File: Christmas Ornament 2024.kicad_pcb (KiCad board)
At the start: 2 copper layers, 76.2 x 76.2 mm, 80 parts, among them J1 USB_B_Micro, J2 Conn_01x03, J3 Conn_01x03, J4 Conn_01x03, J5 Conn_01x03, SW1 PTS815, SW2 PTS815, SW3 PTS815, SW4 PTS815, U1 RP2040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

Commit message: Layout in progress...
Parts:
- J2: footprint Connector_PinHeader_2.54mm:PinHeader_1x03_P2.54mm_Vertical -> Connector_JST:JST_SH_BM03B-SRSS-TB_1x03-1MP_P1.00mm_Vertical
- J3: footprint Connector_PinHeader_2.54mm:PinHeader_1x03_P2.54mm_Vertical -> Connector_PinHeader_1.27mm:PinHeader_1x03_P1.27mm_Vertical
- moved D7 113.1 mm to (93.0, 115.6)
- moved D8 106.8 mm to (113.5, 136.7)
- moved D5 101.2 mm to (90.2, 101.6)
- moved D6 100.1 mm to (101.1, 127.3)
- moved U3 96.4 mm to (115.3, 115.3), turned to 90 degrees
- moved D9 96.4 mm to (126.7, 138.2)
- moved D4 95.5 mm to (93.5, 87.9)
- moved D13 93.2 mm to (140.7, 135.6)
- moved U2 92.9 mm to (127.0, 101.6)
- moved R12 92.7 mm to (104.4, 123.7), turned to 135 degrees
- moved R13 91.3 mm to (97.5, 113.5), turned to 112.5 degrees
- moved R11 90.5 mm to (95.2, 101.3), turned to 90 degrees
- moved D3 86.3 mm to (101.6, 76.5)
- moved R14 85.5 mm to (114.8, 130.8), turned to 157.5 degrees
- moved R10 84.8 mm to (97.8, 89.4), turned to 67.5 degrees
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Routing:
- net GND: track 4.11 -> 42.4 mm
- net QSPI SS: track 0.00 -> 25.0 mm
- net QSPI SD1: track 0.00 -> 20.4 mm
- net QSPI SD2: track 0.00 -> 17.7 mm
- net SWD: track 0.00 -> 15.0 mm
- net SWCLK: track 0.00 -> 14.3 mm
- net QSPI SD3: track 0.00 -> 13.1 mm
- net QSPI SCLK: track 0.00 -> 11.5 mm
- net QSPI SD0: track 0.00 -> 10.5 mm
- net +BATT: track 3.41 -> 12.4 mm
- net TMP235 Out: track 0.00 -> 4.49 mm
- net +3V3: track 39.4 -> 42.6 mm
- net Net-(U5-V_{FB}): track 3.24 -> 4.95 mm
- net Net-(U1-USB_DP): track 4.46 -> 3.84 mm
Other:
- copper layers 2 -> 4

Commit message: PCB Layout and Routing complete
DRC
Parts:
- removed J3: Conn_01x03, Connector_PinHeader_1.27mm:PinHeader_1x03_P1.27mm_Vertical
- added D18: Green LED, LED_SMD:LED_0805_2012Metric_Pad1.15x1.40mm_HandSolder, F.Cu at (124.8, 91.7)
- added R24: 100, Resistor_SMD:R_0805_2012Metric_Pad1.20x1.40mm_HandSolder, F.Cu at (128.9, 91.7)
- JP1: moved to B.Cu
- moved SW3 74.4 mm to (109.1, 130.1), turned to -123.75 degrees
- moved SW2 55.3 mm to (122.1, 63.8), turned to 90 degrees
- moved SW1 46.4 mm to (129.7, 63.8), turned to 90 degrees
- moved SW4 42.3 mm to (146.3, 129.1), turned to -56.25 degrees
- moved JP1 13.6 mm to (130.8, 101.9), turned to 180 degrees
- moved J1 12.8 mm to (127.0, 53.5)
- moved C22 8.41 mm to (137.1, 80.7), turned to 135 degrees
- moved J2 6.40 mm to (148.4, 113.2)
- moved D17 6.01 mm to (127.0, 102.8)
- moved R5 5.69 mm to (127.0, 69.8), turned to 0 degrees
- moved D1 5.65 mm to (127.0, 67.5)
- moved D8 3.66 mm to (113.8, 133.0), turned to 157.5 degrees
- moved C19 3.46 mm to (123.8, 97.2)
- moved U2 3.17 mm to (127.0, 98.4)
- moved D15 2.92 mm to (158.2, 88.5), turned to -67.5 degrees
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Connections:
- U1 pad 3: Net-(J3-Pin_3) -> unconnected-(U1-GPIO1-Pad3)
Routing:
- net BUTTON 2: track 0.00 -> 95.4 mm
- net BUTTON 1: track 0.00 -> 82.2 mm
- net +5V: track 0.00 -> 80.7 mm, vias 0 -> 1
- net LED SSW: track 0.00 -> 66.0 mm
- net GND: track 42.4 -> 102.2 mm, vias 0 -> 52
- net +3V3: track 42.6 -> 100.5 mm, vias 0 -> 19
- net LED SW: track 0.00 -> 56.2 mm
- net LED S: track 0.00 -> 54.5 mm
- net Net-(SW1-A): track 0.00 -> 50.0 mm, vias 0 -> 2
- net LED WSW: track 0.00 -> 48.6 mm
- net LED W: track 0.00 -> 46.4 mm
- net LED N: track 0.00 -> 42.9 mm
- net LED WNW: track 0.00 -> 42.7 mm
- net LED SSE: track 0.00 -> 42.4 mm
- net Net-(J1-D-): track 0.00 -> 40.3 mm
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- added copper zone on In2.Cu, net +3V3
- added copper zone on F.Cu, net GND
- added copper zone on In1.Cu, net GND
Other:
- board size 76.2 x 76.2 mm -> 81.3 x 91.5 mm
- board text added: "To Do: 1. Add mounting holes 2. Top hatched ground pour 3. Silkscreen - Temperature - Christmas Notes - Github Link - Button Labels"

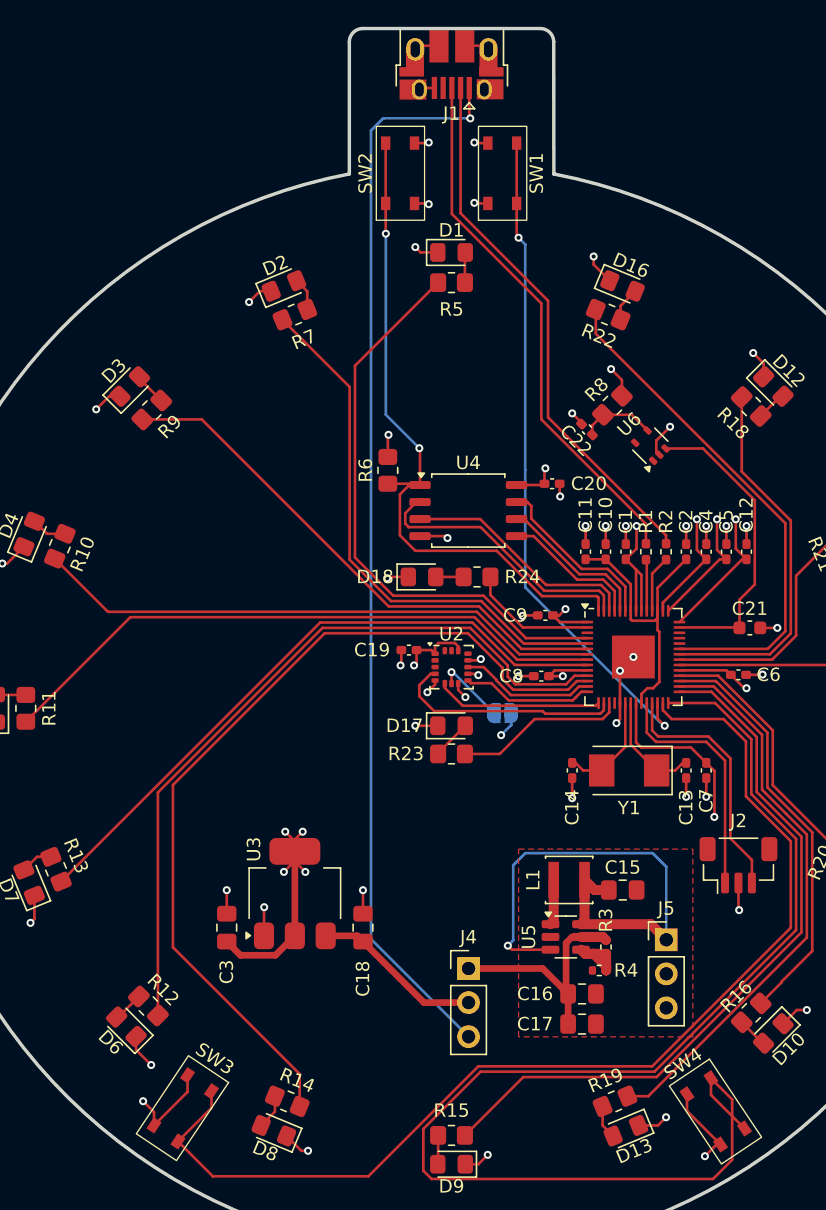
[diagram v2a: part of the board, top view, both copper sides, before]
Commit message: Silkscreen in progress
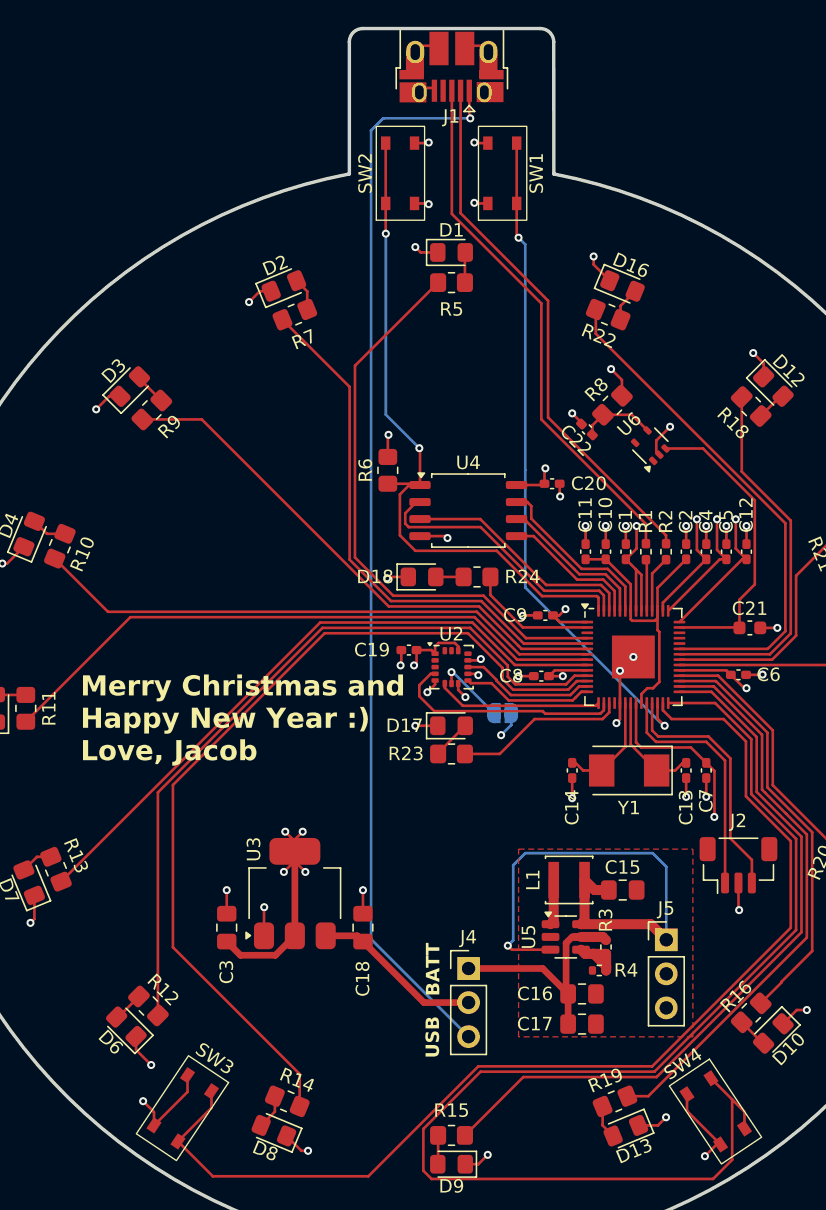
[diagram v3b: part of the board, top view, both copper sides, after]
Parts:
- moved J1 0.21 mm to (127.0, 53.7)
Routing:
- net BUTTON 2: track 95.4 -> 93.1 mm
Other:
- board text added: "BATT"
- board text added: "Christmas Ornament 2024 github.com/jacobantoun"
- board text added: "Merry Christmas and Happy New Year :) Love, Jacob"
- board text added: "Press SW3 to wake up Press SW4 to toggle between spirit level and temperature"
- board text added: "USB"
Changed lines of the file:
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@@
 		(tags "resistor handsolder")
 		(property "Reference" "R23"
-			(at 3.4 0.002001 360)
+			(at 3.4 0.002001 0)
 			(layer "F.SilkS")
 			(effects
@@
 		)
 		(property "Value" "100"
-			(at -0.000001 1.650003 360)
+			(at -0.000001 1.650003 0)
 			(layer "F.Fab")
 			(effects
@@
 		)
 		(fp_text user "${REFERENCE}"
-			(at 0 0 360)
+			(at 0 0 0)
 			(layer "F.Fab")
 			(effects
@@
 		(tags "resistor handsolder")
 		(property "Reference" "R24"
-			(at -3.4 0 360)
+			(at -3.4 0 0)
 			(layer "F.SilkS")
 			(effects
@@
 		)
 		(property "Value" "100"
-			(at -0.000001 1.650003 360)
+			(at -0.000001 1.650003 0)
 			(layer "F.Fab")
 			(effects
@@
 		)
 		(fp_text user "${REFERENCE}"
-			(at 0 0 360)
+			(at 0 0 0)
 			(layer "F.Fab")
 			(effects
@@
 		(tags "resistor handsolder")
 		(property "Reference" "R15"
-			(at 0 1.85 360)
+			(at 0 1.85 0)
 			(layer "F.SilkS")
 			(effects
@@
 		)
 		(property "Value" "100"
-			(at 0 1.65 360)
+			(at 0 1.65 0)
 			(layer "F.Fab")
 			(effects
@@
 		)
 		(fp_text user "${REFERENCE}"
-			(at 0 0 360)
+			(at 0 0 0)
 			(layer "F.Fab")
 			(effects
@@
 		(tags "LED handsolder")
 		(property "Reference" "D9"
-			(at 0 -1.65 360)
+			(at 0 -1.65 0)
 			(layer "F.SilkS")
 			(effects
@@
 		)
 		(property "Value" "Green LED"
-			(at 0 1.65 360)
+			(at 0 1.65 0)
 			(layer "F.Fab")
 			(effects
@@
 		)
 		(fp_text user "${REFERENCE}"
-			(at 0 0 360)
+			(at 0 0 0)
 			(layer "F.Fab")
 			(effects
@@
 	(footprint "Connector_USB:USB_Micro-B_Amphenol_10103594-0001LF_Horizontal"
 		(layer "F.Cu")
-		(at 127 53.467 180)
+		(at 127 53.675 180)
 		(descr "Micro USB Type B 10103594-0001LF, http://cdn.amphenol-icc.com/media/wysiwyg/files/drawing/10103594.pdf")
 		(tags "USB USB_B USB_micro USB_OTG")
 		(property "Reference" "J1"
-			(at 0 -3.683 360)
+			(at 0 -3.683 0)
 			(layer "F.SilkS")
 			(effects
@@
 		)
 		(property "Value" "USB_B_Micro"
-			(at -0.025 4.435 360)
+			(at -0.025 4.435 0)
 			(layer "F.Fab")
 			(effects
@@
 		)
 		(fp_text user "PCB edge"
-			(at -0.025001 2.235 360)
+			(at -0.025001 2.235 0)
 			(layer "Dwgs.User")
 			(effects
@@
 		)
 		(fp_text user "${REFERENCE}"
-			(at -0.025 -0.015 360)
+			(at -0.025 -0.015 0)
 			(layer "F.Fab")
 			(effects
@@
 		(tags "resistor handsolder")
 		(property "Reference" "R14"
-			(at -0.095923 1.728265 157.5)
+			(at -0.095923 1.728266 157.5)
 			(layer "F.SilkS")
 			(effects
@@
 		(layer "User.2")
 	)
+	(gr_text "Christmas Ornament 2024\ngithub.com/jacobantoun"
+		(at 142.2 78.775 0)
+		(layer "B.SilkS")
+		(effects
+			(font
+				(size 1.5 1.5)
+				(thickness 0.25)
+				(bold yes)
+			)
+			(justify left bottom mirror)
+		)
+	)
+	(gr_text "Press SW3 to wake up\nPress SW4 to toggle between \nspirit level and temperature"
+		(at 141.375 110.5 0)
+		(layer "B.SilkS")
+		(effects
+			(font
+				(size 1.5 1.5)
+				(thickness 0.25)
+				(bold yes)
+			)
+			(justify left bottom mirror)
+		)
+	)
+	(gr_text "USB"
+		(at 125.6 126.025 90)
+		(layer "F.SilkS")
+		(effects
+			(font
+				(size 1 1)
+				(thickness 0.2)
+				(bold yes)
+			)
+		)
+	)
+	(gr_text "BATT"
+		(at 125.625 120.975 90)
+		(layer "F.SilkS")
+		(effects
+			(font
+				(size 1 1)
+				(thickness 0.2)
+				(bold yes)
+			)
+		)
+	)
+	(gr_text "Merry Christmas and \nHappy New Year :)\nLove, Jacob"
+		(at 99.325 105.55 0)
+		(layer "F.SilkS")
+		(effects
+			(font
+				(size 1.5 1.5)
+				(thickness 0.25)
+				(bold yes)
+			)
+			(justify left bottom)
+		)
+	)
 	(gr_text "To Do:\n1. Add mounting holes\n2. Top hatched ground pour\n3. Silkscreen\n    - Temperature\n	- Christmas Notes\n	- Github Link\n	- Button Labels"
 		(at 88.2 62.4 0)
@@
 	)
 	(segment
+		(start 148.849649 132.831679)
+		(end 148.849649 131.590132)
+		(width 0.2)
+		(layer "F.Cu")
+		(net 60)
+	)
+	(segment
 		(start 152.7 118.034314)
 		(end 152.7 111.238178)
@@
 	)
 	(segment
-		(start 146.349583 129.090066)
-		(end 146.349583 130.331613)
+		(start 148.849649 131.590132)
+		(end 147.930789 130.671272)
 		(width 0.2)
 		(layer "F.Cu")
@@
 		(width 0.2)
 		(layer "F.Cu")
-		(net 60)
-	)
-	(segment
-		(start 146.349583 130.331613)
-		(end 148.849649 132.831679)
-		(width 0.2)
-		(layer "F.Cu")

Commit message: BOM and Gerber export
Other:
- board text removed: "To Do: 1. Add mounting holes 2. Top hatched ground pour 3. Silkscreen - Temperature - Christmas Notes - Github Link - Button Labels"
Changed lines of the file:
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@@
 			(outputformat 1)
 			(mirror no)
-			(drillshape 1)
+			(drillshape 0)
 			(scaleselection 1)
-			(outputdirectory "")
+			(outputdirectory "Gerbers/")
 		)
 	)
@@
 			)
 			(justify left bottom)
-		)
-	)
-	(gr_text "To Do:\n1. Add mounting holes\n2. Top hatched ground pour\n3. Silkscreen\n    - Temperature\n	- Christmas Notes\n	- Github Link\n	- Button Labels"
-		(at 88.2 62.4 0)
-		(layer "Cmts.User")
-		(effects
-			(font
-				(size 1 1)
-				(thickness 0.15)
-			)
-			(justify left bottom)

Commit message: BOM and CPL ready for ordering
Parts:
- added H1: MountingHole, MountingHole:MountingHole_2.1mm, F.Cu at (132.5, 52.8)
- added H2: MountingHole, MountingHole:MountingHole_2.1mm, F.Cu at (121.4, 52.7)
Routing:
- net BUTTON 2: track 93.1 -> 94.4 mm
- net GND: track 102.2 -> 103.0 mm
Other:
- board text added: "+Vin"
- board text added: "54°F"
- board text added: "56°F"
- board text added: "58°F"
- board text added: "60°F"
- board text added: "62°F"
- board text added: "64°F"
- board text added: "66°F"
- board text added: "68°F"
- board text added: "70°F"
- board text added: "72°F"
- board text added: "74°F"
- board text added: "76°F"
- board text added: "78°F"
- board text added: "80°F"
- board text added: "82°F"
- board text added: "Gnd"
- board text added: "Important Pinouts: LIS3DH I2C SDA -> GPIO12 (I2C0) LIS3DH I2C SCL -> GPIO13 (I2C0) Wake Button -> GPIO16 Mode Button -> GPIO17 TMP235 Vout -> GPIO29 (ADC3) Heartbeat LED -> GPIO0"
- board text added: "Merry Christmas and Happy New Year :) - Jacob Antoun"
- board text added: "Mode"
- board text added: "PROG"
- board text added: "RST"
- board text added: "Wake up!"
- board text added: "maybe the first dual-core christmas ornament???"
- board text removed: "Merry Christmas and Happy New Year :) Love, Jacob"
- board text removed: "Press SW3 to wake up Press SW4 to toggle between spirit level and temperature"
